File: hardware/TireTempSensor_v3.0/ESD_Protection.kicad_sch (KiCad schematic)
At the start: 6 parts

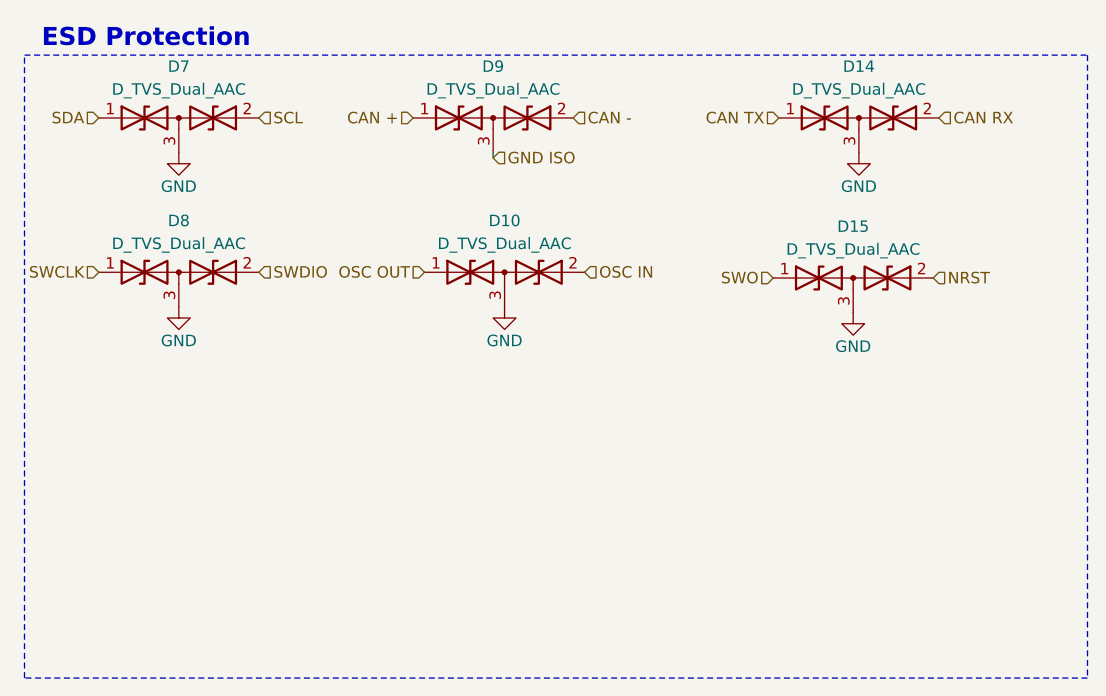
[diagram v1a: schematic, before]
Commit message: Nowy layout, nowe tvsy
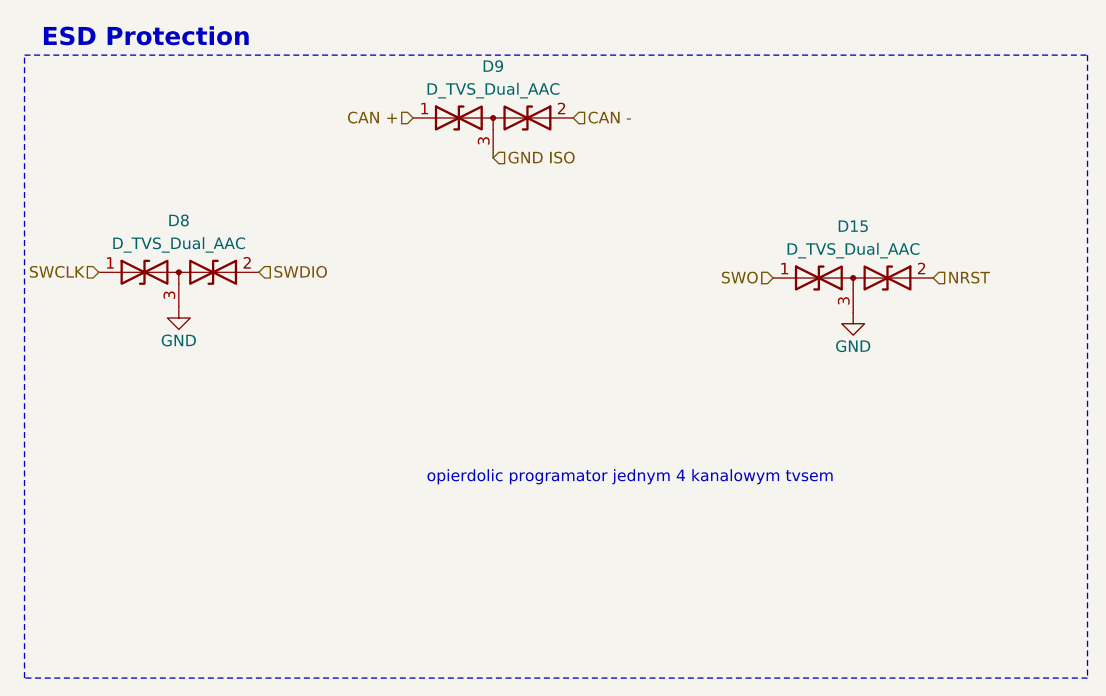
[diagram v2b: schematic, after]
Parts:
- removed D10, D14, D7: D_TVS_Dual_AAC, Package_TO_SOT_SMD:SOT-23_Handsoldering, symbol Device:D_TVS_Dual_AAC
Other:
- note added: "opierdolic programator jednym 4 kanalowym tvsem"
